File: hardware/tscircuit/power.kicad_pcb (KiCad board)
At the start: 2 copper layers, 90 x 70 mm, 27 parts, among them SW1 10mΩ

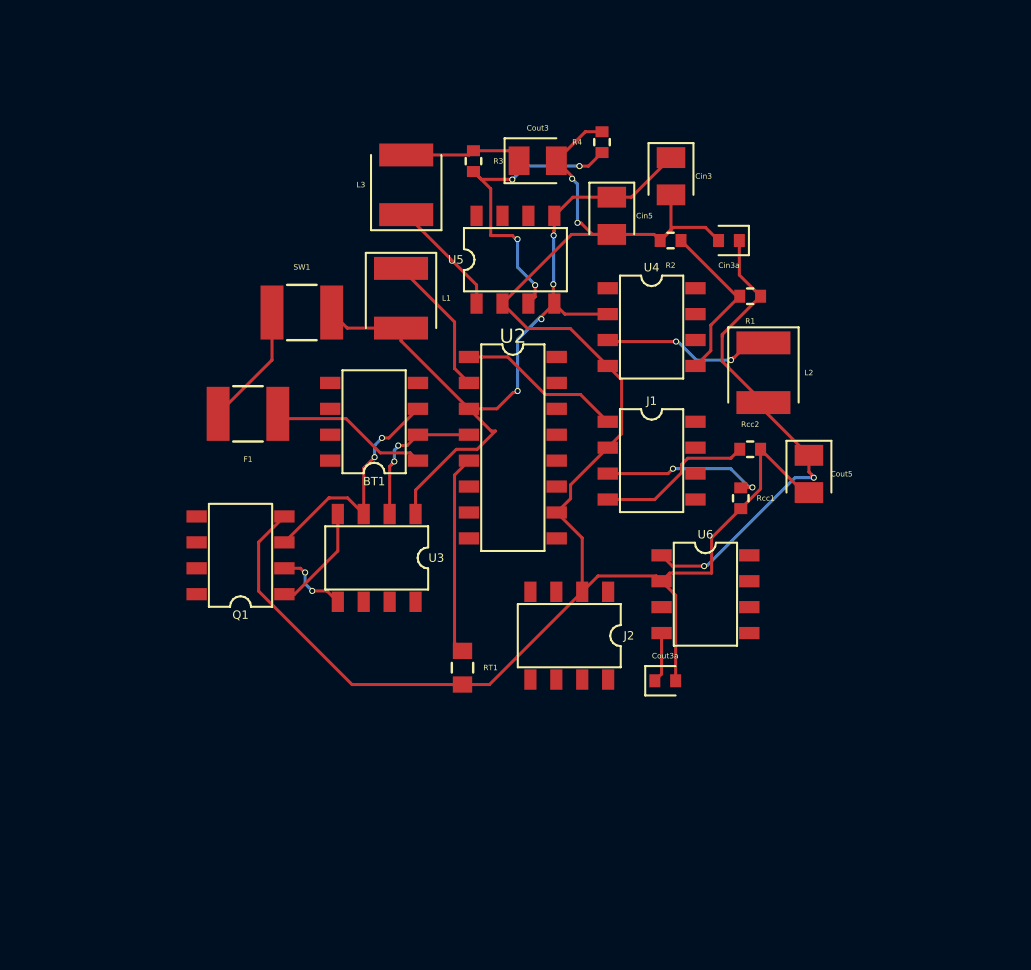
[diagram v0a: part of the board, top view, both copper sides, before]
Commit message: hw(power): realize sheet to fab-draft — engine-pulled footprints, boost topology fix
power.tsx now uses manufacturer-verified footprints + pinouts pulled from the
LCSC/JLCPCB database by part number (footprint="jlcpcb:C…"), so pinouts are
authoritative, not hand-typed. KiCad DRC on the export: 0 unconnected, 0 shorts,
0 schematic-parity (remaining violations are placement/routing only).

- BQ25887 rewired as the BOOST it is: inductor PMID<->SW, boost output SNS->BAT,
  full support net (PMID/REGN/BTST/SNS/ILIM/MID caps) + TS thermistor divider from
  REGN (missing before -> charging would be blocked). Was buck-style SW->L->BAT.
- MP2315 on its authoritative pinout (1 AAM,2 IN,3 SW,4 GND,5 BST,6 EN,7 VCC,8 FB);
  added VCC decouple + AAM. (An earlier hand-typed draft had this pinout wrong.)
- S-8252A reference sides corrected (VSS=B-, VM=EB-) + VDD/VC RC network.
- 2S protection FETs: standard back-to-back common-drain pair (2x AO3400A).
- USB-C real 16P receptacle (C2988369; C165948 shell pads render NaN, avoided).

LCSC: BQ25887 C2761614, MP2315 C45889, TPS7A2033 C2862740, S-8252A C468224,
AO3400A C20917, USB-C C2988369. Docs (EN+RU) synced. board.tsx (combined) is still
pre-realization and will be regenerated once all 6 sheets are realized.

Co-Authored-By: Claude Opus 4.8 <noreply@anthropic.com>
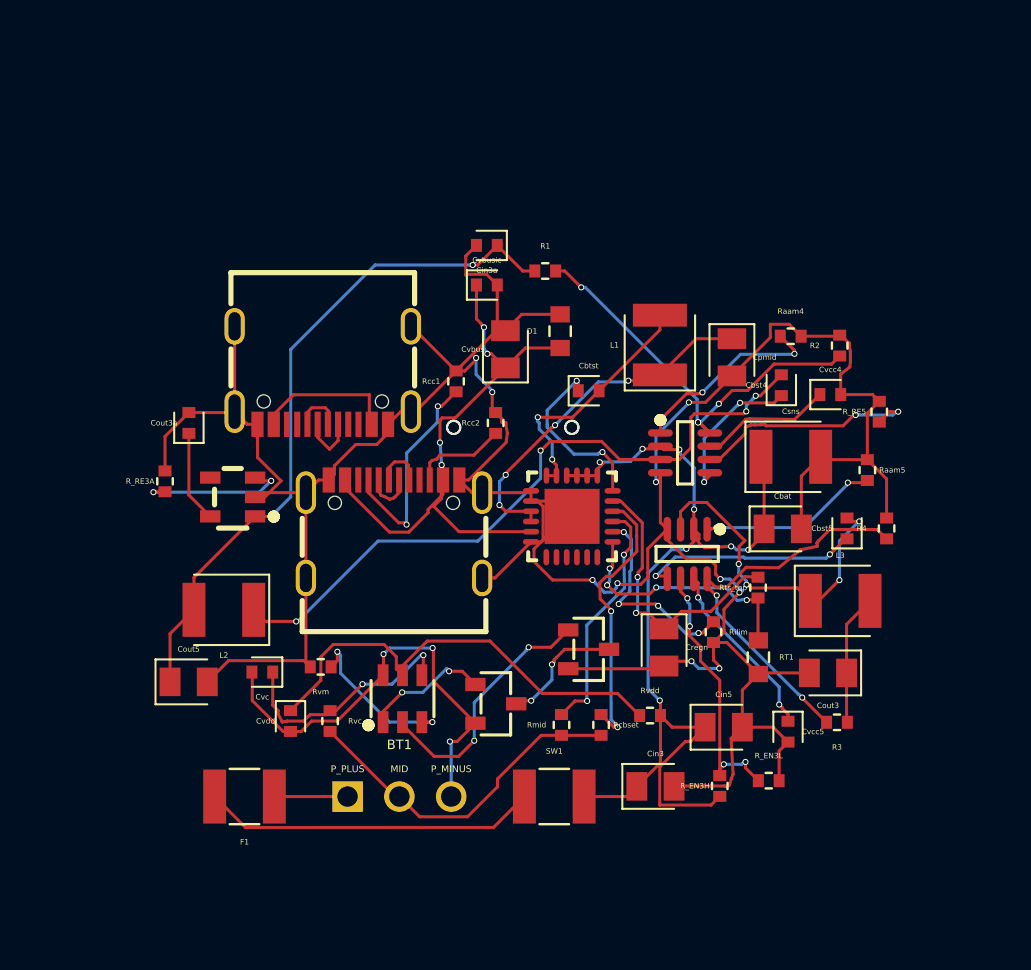
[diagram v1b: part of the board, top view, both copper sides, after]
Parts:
- added Cbat: 10uF, tscircuit:capacitor_cap0805, F.Cu at (113.2, 104.0)
- added Cbst4: 100nF, tscircuit:capacitor_cap0402, F.Cu at (113.2, 96.9)
- added Cbst5: 100nF, tscircuit:capacitor_cap0402, F.Cu at (116.4, 104.0)
- added Cbtst: 47nF, tscircuit:capacitor_cap0402, F.Cu at (103.7, 97.2)
- added Cpmid: 10uF, tscircuit:capacitor_cap0805, F.Cu at (110.7, 95.6)
- added Cregn: 4.7uF, tscircuit:capacitor_cap0805, F.Cu at (107.4, 109.8)
- added Csns: 47uF, tscircuit:capacitor_cap1210, F.Cu at (113.6, 100.4)
- added Cvbus: 10uF, tscircuit:capacitor_cap0805, F.Cu at (99.6, 95.2)
- added Cvbusic: 1uF, tscircuit:capacitor_cap0402, F.Cu at (98.7, 92.0)
- added Cvc: 0.1uF, tscircuit:capacitor_cap0402, F.Cu at (87.7, 111.0)
- added Cvcc4: 0.1uF, tscircuit:capacitor_cap0402, F.Cu at (115.6, 97.4)
- added Cvcc5: 0.1uF, tscircuit:capacitor_cap0402, F.Cu at (113.5, 113.9)
- added Cvdd: 0.1uF, tscircuit:capacitor_cap0402, F.Cu at (89.1, 113.4)
- added D1: 1MΩ, tscircuit:resistor_res0603, F.Cu at (102.3, 94.3)
- added Q2: , tscircuit:chip, F.Cu at (103.7, 109.9)
- added R_EN3H: 100kΩ, tscircuit:resistor_res0402, F.Cu at (110.1, 116.6)
- added R_EN3L: 47kΩ, tscircuit:resistor_res0402, F.Cu at (112.5, 116.3)
- added R_RE3A: 100kΩ, tscircuit:resistor_res0402, F.Cu at (83.0, 101.6)
- added R_RE5: 100kΩ, tscircuit:resistor_res0402, F.Cu at (118.0, 98.2)
- added Raam4: 100kΩ, tscircuit:resistor_res0402, F.Cu at (113.6, 94.5)
- added Raam5: 100kΩ, tscircuit:resistor_res0402, F.Cu at (117.4, 101.1)
- added Rcbset: 10Ω, tscircuit:resistor_res0402, F.Cu at (104.3, 113.6)
- added Rilim: 383Ω, tscircuit:resistor_res0402, F.Cu at (109.8, 109.0)
- added Rmid: 300Ω, tscircuit:resistor_res0402, F.Cu at (102.4, 113.6)
- added Rts_top: 5.23kΩ, tscircuit:resistor_res0402, F.Cu at (112.0, 106.9)
- added Rvc: 470Ω, tscircuit:resistor_res0402, F.Cu at (91.0, 113.4)
- added Rvdd: 470Ω, tscircuit:resistor_res0402, F.Cu at (106.7, 113.1)
- added Rvm: 2kΩ, tscircuit:resistor_res0402, F.Cu at (90.6, 110.7)
- BT1: footprint tscircuit:chip_soic8 -> tscircuit:chip_pinrow3
- J1, J2, Q1, U3, U4, U5, U6: footprint tscircuit:chip_soic8 -> tscircuit:chip
- R3: value 45.3kΩ -> 31.6kΩ
- U2: footprint tscircuit:chip_soic16 -> tscircuit:chip
- moved R3 32.8 mm to (115.9, 113.5), turned to 180 degrees
- moved Cout5 32.1 mm to (84.1, 111.5), turned to 0 degrees
- moved Cin3 29.9 mm to (107.0, 116.6), turned to 0 degrees
- moved L3 29.5 mm to (116.0, 107.5), turned to 0 degrees
- moved L2 28.9 mm to (85.8, 107.9), turned to 180 degrees
- moved Cout3 28.8 mm to (115.4, 111.0), turned to 180 degrees
- moved SW1 26.8 mm to (102.0, 117.1)
- moved Cout3a 26.5 mm to (84.1, 98.8), turned to 90 degrees
- moved Cin5 25.7 mm to (110.3, 113.7), turned to 0 degrees
- moved U6 23.7 mm to (86.3, 102.4)
- moved R4 23.5 mm to (118.3, 104.0)
- moved F1 18.8 mm to (86.8, 117.1)
- moved BT1 18.4 mm to (94.4, 117.1), turned to 0 degrees
- moved J2 17.7 mm to (90.7, 96.3), turned to 180 degrees
- moved U5 16.7 mm to (108.5, 105.2)
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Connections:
- BT1 pad 3: .BT1 > .P_MINUS to .Q1 > .D -> BMINUS
- J1 pad 1: VBUS_S3 -> GND
- J1 pad 3: .Rcc1 > .pin1 to .J1 > .CC1 -> GND
- J1 pad 4: .Rcc2 > .pin1 to .J1 > .CC2 -> GND
- J1 pad 5: USB_DP_S3 -> GND
- J1 pad 6: USB_DM_S3 -> VBUS_S3
- J1 pad 7: (no net) -> .Rcc2 > .pin1 to .J1 > .CC2
- J2 pad 1: VBUS_C5 -> GND
- J2 pad 3: (no net) -> GND
- J2 pad 4: (no net) -> GND
- J2 pad 5: USB_DP_C5 -> GND
- J2 pad 6: USB_DM_C5 -> VBUS_C5
- L1 pad 1: .U2 > .SW to .L1 > .pin1 -> PMID
- L1 pad 2: BAT -> SW
- Q1 pad 1: .U3 > .DO to .Q1 > .G1 -> .U3 > .DO to .Q1 > .G
- Q1 pad 2: .U3 > .CO to .Q1 > .G2 -> BMINUS
- Q1 pad 3: .BT1 > .P_MINUS to .Q1 > .D -> PACKMID
- U2 pad 1: VBUS_S3 -> (no net)
- U2 pad 10: GND -> .Rcbset > .pin1 to .U2 > .CBSET
- U2 pad 11: (no net) -> .Cregn > .pin1 to .U2 > .REGN
- U2 pad 12: (no net) -> .Cbtst > .pin1 to .U2 > .BTST
- U2 pad 13: (no net) -> BAT
- U2 pad 14: (no net) -> BAT
- U2 pad 15: (no net) -> BAT
- U2 pad 16: (no net) -> BAT
- U2 pad 2: .U2 > .SW to .L1 > .pin1 -> (no net)
- U2 pad 3: BAT -> BQ_CD
- U2 pad 4: BATM -> I2C_SDA
- U2 pad 5: TS -> I2C_SCL
- U2 pad 6: I2C_SDA -> BQ_INT
- U2 pad 7: I2C_SCL -> TS
- U2 pad 8: BQ_CD -> .Rilim > .pin1 to .U2 > .ILIM
- U2 pad 9: BQ_INT -> .Rmid > .pin1 to .U2 > .MID
- U3 pad 1: BAT -> .U3 > .DO to .Q1 > .G
- U3 pad 2: BATM -> .U3 > .CO to .Q2 > .G
- U3 pad 3: .BT1 > .P_MINUS to .Q1 > .D -> .Rvm > .pin1 to .U3 > .VM
- U3 pad 4: .U3 > .DO to .Q1 > .G1 -> .Rvc > .pin1 to .U3 > .VC
- U3 pad 5: .U3 > .CO to .Q1 > .G2 -> .Rvdd > .pin1 to .U3 > .VDD
- U3 pad 6: (no net) -> BMINUS
- U4 pad 1: (no net) -> .Raam4 > .pin1 to .U4 > .AAM
- U4 pad 5: .R1 > .pin2 to .U4 > .FB -> .Cbst4 > .pin1 to .U4 > .BST
- U4 pad 7: (no net) -> .Cvcc4 > .pin1 to .U4 > .VCC
- U4 pad 8: (no net) -> .R1 > .pin2 to .U4 > .FB
- U5 pad 1: .U5 > .SW to .L3 > .pin1 -> .Raam5 > .pin1 to .U5 > .AAM
- U5 pad 2: GND -> BAT
- U5 pad 3: .R3 > .pin2 to .U5 > .FB -> .U5 > .SW to .L3 > .pin1
- U5 pad 4: BAT -> GND
- U5 pad 5: BAT -> .Cbst5 > .pin1 to .U5 > .BST
- U5 pad 6: (no net) -> .R_EN3H > .pin2 to .U5 > .pin6
- U5 pad 7: (no net) -> .Cvcc5 > .pin1 to .U5 > .VCC
- U5 pad 8: (no net) -> .R3 > .pin2 to .U5 > .FB
- U6 pad 4: V3V3A -> (no net)
- U6 pad 5: (no net) -> V3V3A
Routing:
- net GND: track 89.2 -> 165.0 mm, vias 2 -> 10
- net .U4 > .SW to .L2 > .pin1: track 8.40 -> 33.7 mm, vias 2 -> 4
- net .Rvdd > .pin1 to .U3 > .VDD: track 0.00 -> 22.6 mm
- net BMINUS: track 0.00 -> 22.1 mm, vias 0 -> 3
- net VBUS_S3: track 8.12 -> 29.7 mm, vias 0 -> 4
- net PMID: track 0.00 -> 17.7 mm, vias 0 -> 4
- net .Cregn > .pin1 to .U2 > .REGN: track 0.00 -> 13.8 mm, vias 0 -> 2
- net .Rcbset > .pin1 to .U2 > .CBSET: track 0.00 -> 13.7 mm, vias 0 -> 2
- net .R_EN3H > .pin2 to .U5 > .pin6: track 0.00 -> 13.4 mm, vias 0 -> 4
- net .U3 > .CO to .Q2 > .G: track 0.00 -> 12.6 mm, vias 0 -> 2
- net .R1 > .pin2 to .U4 > .FB: track 8.33 -> 20.6 mm, vias 0 -> 4
- net SW: track 0.00 -> 12.2 mm, vias 0 -> 2
- net .Rmid > .pin1 to .U2 > .MID: track 0.00 -> 12.0 mm, vias 0 -> 2
- net .Rvc > .pin1 to .U3 > .VC: track 0.00 -> 11.9 mm, vias 0 -> 2
- net .BT1 > .P_MINUS to .Q1 > .D: track 11.6 -> 0.00 mm, vias 2 -> 0
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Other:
- outline, holes or cut-outs redrawn

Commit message: hw: fix 6 issues from realized-board self-review (2 blockers)
Adversarial multi-agent review of the real-parts board caught 6 real defects the
per-sheet DRC couldn't see; all datasheet-verified, fixed, sheets re-verified
(DRC parity=0 each):

- BLOCKER (power): BQ25887 SNS was tied to BAT externally -> shorts the internal
  charge-current shunt, defeating ICHG regulation on the 2S pack. SNS is now its own
  net (44uF to GND only); the SNS<->BAT shunt is internal.
- BLOCKER (expansion): PESD5V0S2UAT ESD arrays (common-cathode) had the common cathode
  on GND -> every I2C logic-high forward-biases the diode and clamps SDA/SCL to ~0.6V
  (whole bus dead). Cathode moved to +3V3 (clamps overshoot above the rail).
- MAJOR (audio): PAM8302 inputs were DC-coupled (IN- hard to GND) -> breaks the
  internal VDD/2 bias and rails the output. Added series 0.1uF caps on both inputs.
- MINOR (power): BQ25887 TS divider was missing RT2 (30.1k || NTC) -> shifted temp
  window; added.
- MINOR (power): MP2315 bootstraps were missing the datasheet-required 20R series
  resistor; added Rbst4/Rbst5.
- MINOR (rf): SP4T pins 1/8/11/12/14 are N/C per the SKY13414 datasheet -> untied from
  GND (only the EP paddle is ground).

GPIO45 (VDD_SPI strap on CC1101 GDO2) is handled by the set_flash_voltage eFuse (a
verifier false-positive) -> documented inline. Docs (power EN+RU) corrected.

Co-Authored-By: Claude Opus 4.8 <noreply@anthropic.com>
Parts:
- added RT2: 30.1kΩ, tscircuit:resistor_res0402, F.Cu at (114.2, 106.8)
- added Rbst4: 20Ω, tscircuit:resistor_res0402, F.Cu at (115.1, 96.9)
- added Rbst5: 20Ω, tscircuit:resistor_res0402, F.Cu at (114.7, 111.1)
- moved Cout3 10.5 mm to (118.6, 101.0)
- moved Raam5 6.95 mm to (117.1, 108.0), turned to -90 degrees
- moved R3 6.90 mm to (119.5, 107.6)
- moved R4 6.52 mm to (117.6, 110.4), turned to 0 degrees
- moved Cbst5 5.48 mm to (114.7, 109.2), turned to 0 degrees
- moved Cvcc4 4.16 mm to (113.2, 94.0), turned to 90 degrees
- moved R_EN3L 4.02 mm to (115.4, 113.5), turned to -90 degrees
- moved L3 3.67 mm to (118.2, 104.5)
- moved Raam4 3.64 mm to (110.7, 92.3)
- moved R2 1.36 mm to (115.1, 94.0)
- moved R_EN3H 0.71 mm to (110.6, 116.0), turned to 180 degrees
- moved R_RE5 0.36 mm to (117.8, 98.6), turned to 0 degrees
- moved Cvcc5 0.32 mm to (113.5, 113.6)
- moved Cbat 0.08 mm to (113.2, 103.9)
- moved Cbst4 0.08 mm to (113.2, 96.9)
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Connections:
- Cbst4 pad 2: .U4 > .SW to .L2 > .pin1 -> .Cbst4 > .pin2 to .Rbst4 > .pin1
- Cbst5 pad 2: .U5 > .SW to .L3 > .pin1 -> .Cbst5 > .pin2 to .Rbst5 > .pin1
- Csns pad 1: BAT -> SNS
- U2 pad 15: BAT -> SNS
- U2 pad 16: BAT -> SNS
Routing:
- net SNS: track 0.00 -> 12.6 mm, vias 0 -> 2
- net .Rcc1 > .pin1 to .J1 > .CC1: track 10.8 -> 20.1 mm, vias 2 -> 6
- net .R_EN3H > .pin2 to .U5 > .pin6: track 13.4 -> 20.2 mm, vias 4 -> 2
- net GND: track 165.0 -> 158.3 mm, vias 10 -> 6
- net BAT: track 47.4 -> 41.9 mm, vias 8 -> 4
- net .U5 > .SW to .L3 > .pin1: track 16.7 -> 21.5 mm
- net .Cbst5 > .pin2 to .Rbst5 > .pin1: track 0.00 -> 4.17 mm, vias 0 -> 2
- net .U4 > .SW to .L2 > .pin1: track 33.7 -> 37.8 mm
- net .R3 > .pin2 to .U5 > .FB: track 19.9 -> 15.8 mm, vias 2 -> 4
- net .Raam5 > .pin1 to .U5 > .AAM: track 8.88 -> 12.2 mm
- net PACKMID: track 6.17 -> 9.21 mm
- net .Rcc2 > .pin1 to .J1 > .CC2: track 4.67 -> 7.42 mm, vias 0 -> 2
- net .Rvdd > .pin1 to .U3 > .VDD: track 22.6 -> 19.9 mm
- net BMINUS: track 22.1 -> 19.6 mm, vias 3 -> 2
- net .Cregn > .pin1 to .U2 > .REGN: track 13.8 -> 16.0 mm
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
